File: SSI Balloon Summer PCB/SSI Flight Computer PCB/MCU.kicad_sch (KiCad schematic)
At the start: 27 parts, among them J5 Conn_01x05, J9 Camera, SW2 SW_SPST, SW3 SW_SPST, U7 STM32F411CEUx, Y1 ABM8W-12.0000MHZ-8-K1Z-T3

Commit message: Various rewiring: SWD, microSD, APRS JST
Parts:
- J5: value Conn_01x05 -> SWDIO
- SW1: renamed from SW2; value SW_SPST -> NRST
- SW2: renamed from SW3; value SW_SPST -> BOOT0
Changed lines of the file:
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@@
 			)
 		)
-		(property "Value" "Conn_01x05"
+		(property "Value" "SWDIO"
 			(at 292.1 210.82 0)
 			(show_name no)
@@
 		(dnp no)
 		(fields_autoplaced yes)
-		(property "Reference" "SW2"
+		(property "Reference" "SW1"
 			(at 349.25 218.4399 90)
 			(show_name no)
@@
 			)
 		)
-		(property "Value" "SW_SPST"
+		(property "Value" "NRST"
 			(at 349.25 220.9799 90)
 			(show_name no)
@@
 			(project "SSI Summer Balloons"
 				(path "/3c45a535-6e6b-4825-ad52-82c10cbe7866/b11ef58b-98ba-47ea-88cc-0eee30828228"
-					(reference "SW2")
+					(reference "SW1")
 					(unit 1)
 				)
@@
 		(dnp no)
 		(fields_autoplaced yes)
-		(property "Reference" "SW3"
+		(property "Reference" "SW2"
 			(at 379.73 209.5499 90)
 			(show_name no)
@@
 			)
 		)
-		(property "Value" "SW_SPST"
+		(property "Value" "BOOT0"
 			(at 379.73 212.0899 90)
 			(show_name no)
@@
 			(project "SSI Summer Balloons"
 				(path "/3c45a535-6e6b-4825-ad52-82c10cbe7866/b11ef58b-98ba-47ea-88cc-0eee30828228"
-					(reference "SW3")
+					(reference "SW2")
 					(unit 1)
 				)

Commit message: Cleaned APRS Filter up and adding Testing points
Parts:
- removed C48: 1nF, Capacitor_SMD:C_0603_1608Metric, symbol Device:C
- removed R31: 47k, Resistor_SMD:R_0603_1608Metric, symbol Device:R
- added TP10, TP5, TP6, TP9: TestPoint, TestPoint:TestPoint_Pad_1.5x1.5mm, symbol Connector:TestPoint
- C47: value 10nF -> 22nF
- R30: value 4.7k -> 1k
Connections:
- net APRS_AUDIO: now also C47.1, R30.2, TP6.1
- net GND: now also TP5.1
- net NRST: now also TP10.1
- net APRS_PWM: now reaches R30.1, U7.10 (PA0)
- net APRS_PWM: now also TP9.1
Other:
- moved on the sheet: C47, R30

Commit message: Finished test points
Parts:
- added TP14, TP15: TestPoint, TestPoint:TestPoint_Pad_1.5x1.5mm, symbol Connector:TestPoint
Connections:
- net APRS_PD: now also TP14.1
- net APRS_PTT: now also TP15.1
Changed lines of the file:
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@@
 	(wire
 		(pts
+			(xy 306.07 144.78) (xy 306.07 151.13)
+		)
+		(stroke
+			(width 0)
+			(type default)
+		)
+	)
+	(wire
+		(pts
 			(xy 334.01 34.29) (xy 340.36 34.29)
 		)
@@
 	(wire
 		(pts
+			(xy 289.56 144.78) (xy 289.56 151.13)
+		)
+		(stroke
+			(width 0)
+			(type default)
+		)
+	)
+	(wire
+		(pts
 			(xy 90.17 132.08) (xy 128.27 132.08)
 		)
@@
 		)
 	)
+	(label "APRS_PD"
+		(at 289.56 151.13 0)
+		(effects
+			(font
+				(size 1.27 1.27)
+			)
+			(justify left bottom)
+		)
+	)
 	(label "SCK"
 		(at 180.34 101.6 0)
@@
 		)
 	)
+	(label "APRS_PTT"
+		(at 306.07 151.13 0)
+		(effects
+			(font
+				(size 1.27 1.27)
+			)
+			(justify left bottom)
+		)
+	)
 	(hierarchical_label "MOSI"
 		(shape output)
@@
 	)
 	(symbol
+		(lib_id "Connector:TestPoint")
+		(at 289.56 144.78 0)
+		(unit 1)
+		(body_style 1)
+		(exclude_from_sim no)
+		(in_bom yes)
+		(on_board yes)
+		(in_pos_files yes)
+		(dnp no)
+		(fields_autoplaced yes)
+		(property "Reference" "TP14"
+			(at 292.1 140.2079 0)
+			(show_name no)
+			(do_not_autoplace no)
+			(effects
+				(font
+					(size 1.27 1.27)
+				)
+				(justify left)
+			)
+		)
+		(property "Value" "TestPoint"
+			(at 292.1 142.7479 0)
+			(show_name no)
+			(do_not_autoplace no)
+			(effects
+				(font
+					(size 1.27 1.27)
+				)
+				(justify left)
+			)
+		)
+		(property "Footprint" "TestPoint:TestPoint_Pad_1.5x1.5mm"
+			(at 294.64 144.78 0)
+			(hide yes)
+			(show_name no)
+			(do_not_autoplace no)
+			(effects
+				(font
+					(size 1.27 1.27)
+				)
+			)
+		)
+		(property "Datasheet" ""
+			(at 294.64 144.78 0)
+			(hide yes)
+			(show_name no)
+			(do_not_autoplace no)
+			(effects
+				(font
+					(size 1.27 1.27)
+				)
+			)
+		)
+		(property "Description" "test point"
+			(at 289.56 144.78 0)
+			(hide yes)
+			(show_name no)
+			(do_not_autoplace no)
+			(effects
+				(font
+					(size 1.27 1.27)
+				)
+			)
+		)
+		(property "PART_REV" ""
+			(at 289.56 144.78 0)
+			(hide yes)
+			(show_name no)
+			(do_not_autoplace no)
+			(effects
+				(font
+					(size 1.27 1.27)
+				)
+			)
+		)
+		(pin "1"
+		)
+		(instances
+			(project "SSI Summer Balloons"
+				(path "/3c45a535-6e6b-4825-ad52-82c10cbe7866/b11ef58b-98ba-47ea-88cc-0eee30828228"
+					(reference "TP14")
+					(unit 1)
+				)
+			)
+		)
+	)
+	(symbol
 		(lib_id "Device:C")
 		(at 191.77 68.58 0)
@@
 					(unit 1)
 				)
+			)
+		)
+	)
+	(symbol
+		(lib_id "Connector:TestPoint")
+		(at 306.07 144.78 0)
+		(unit 1)
+		(body_style 1)
+		(exclude_from_sim no)
+		(in_bom yes)
+		(on_board yes)
+		(in_pos_files yes)
+		(dnp no)
+		(fields_autoplaced yes)
+		(property "Reference" "TP15"
+			(at 308.61 140.2079 0)
+			(show_name no)
+			(do_not_autoplace no)
+			(effects
+				(font
+					(size 1.27 1.27)
+				)
+				(justify left)
+			)
+		)
+		(property "Value" "TestPoint"
+			(at 308.61 142.7479 0)
+			(show_name no)
+			(do_not_autoplace no)
+			(effects
+				(font
+					(size 1.27 1.27)
+				)
+				(justify left)
+			)
+		)
+		(property "Footprint" "TestPoint:TestPoint_Pad_1.5x1.5mm"
+			(at 311.15 144.78 0)
+			(hide yes)
+			(show_name no)
+			(do_not_autoplace no)
+			(effects
+				(font
+					(size 1.27 1.27)
+				)
+			)
+		)
+		(property "Datasheet" ""
+			(at 311.15 144.78 0)
+			(hide yes)
+			(show_name no)
+			(do_not_autoplace no)
+			(effects
+				(font
+					(size 1.27 1.27)
+				)
+			)
+		)
+		(property "Description" "test point"
+			(at 306.07 144.78 0)
+			(hide yes)
+			(show_name no)
+			(do_not_autoplace no)
+			(effects
+				(font
+					(size 1.27 1.27)
+				)
+			)
+		)
+		(property "PART_REV" ""
+			(at 306.07 144.78 0)
+			(hide yes)
+			(show_name no)
+			(do_not_autoplace no)
+			(effects
+				(font
+					(size 1.27 1.27)
+				)
+			)
+		)
+		(pin "1"
+		)
+		(instances
+			(project "SSI Summer Balloons"
+				(path "/3c45a535-6e6b-4825-ad52-82c10cbe7866/b11ef58b-98ba-47ea-88cc-0eee30828228"
+					(reference "TP15")
+					(unit 1)
+				)

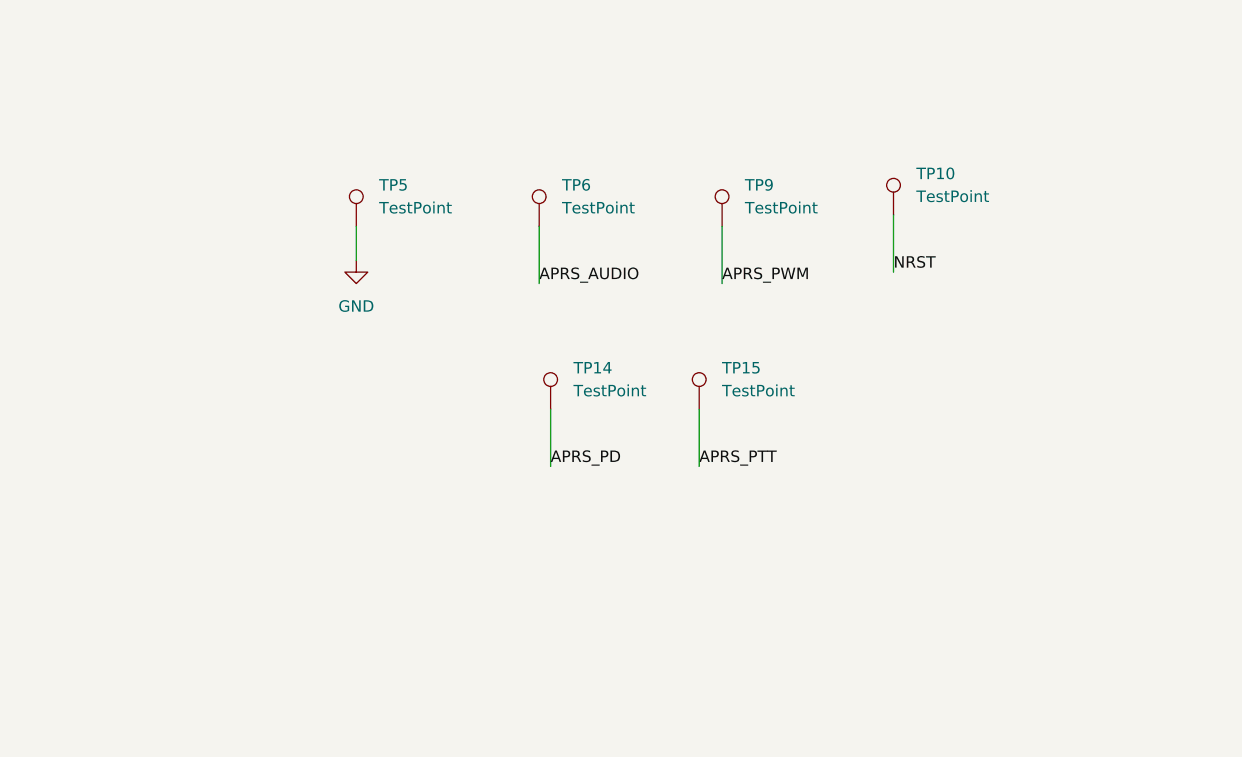
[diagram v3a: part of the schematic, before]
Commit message: Added Headers for testing, finalizing PCB
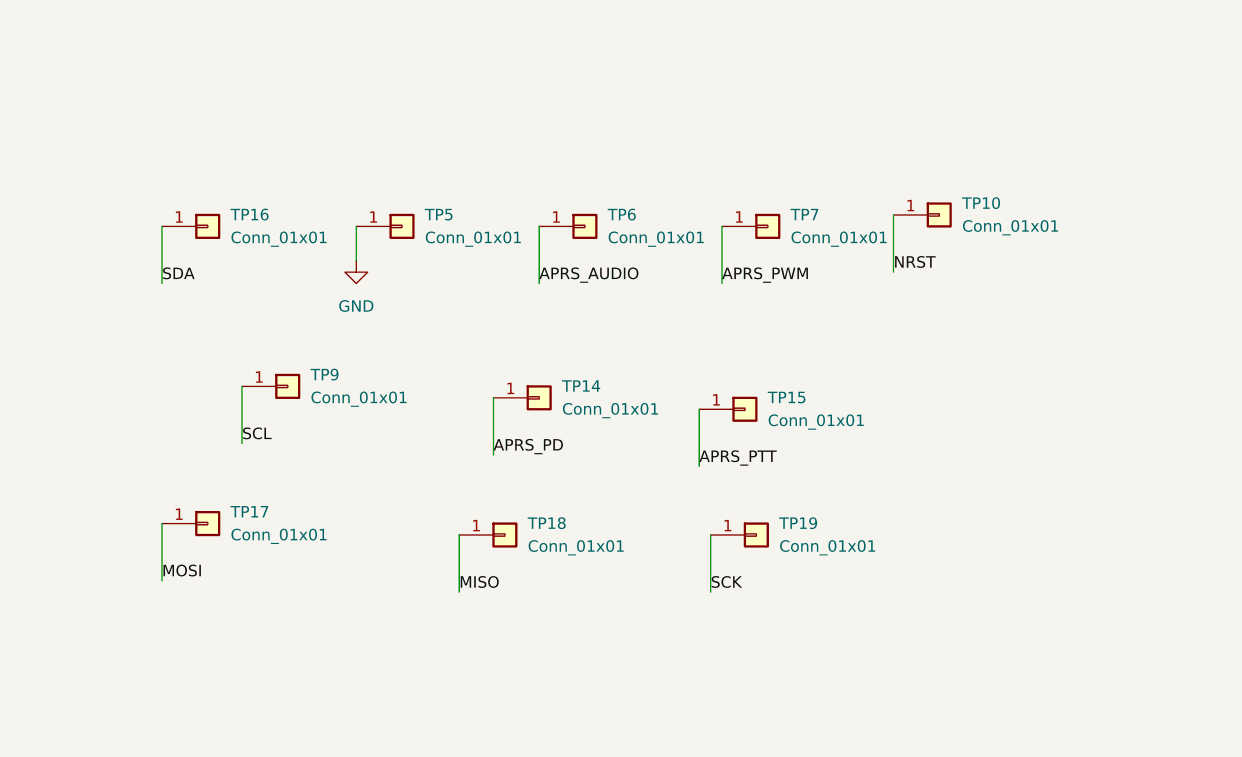
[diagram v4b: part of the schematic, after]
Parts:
- removed TP10, TP14, TP15, TP5, TP6, TP9: TestPoint, TestPoint:TestPoint_Pad_1.5x1.5mm, symbol Connector:TestPoint
- added TP10, TP14, TP15, TP16, TP17, TP18, TP19, TP5, TP6, TP7, TP9: Conn_01x01, Connector_PinHeader_2.54mm:PinHeader_1x01_P2.54mm_Vertical, symbol Connector_Generic:Conn_01x01
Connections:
- net APRS_AUDIO: now also TP6.1 (Pin_1)
- net APRS_PD: now also TP14.1 (Pin_1)
- net APRS_PTT: now also TP15.1 (Pin_1)
- net APRS_PWM: now also TP7.1 (Pin_1)
- net GND: now also TP5.1 (Pin_1)
- net MISO: now also TP18.1 (Pin_1)
- net MOSI: now also TP17.1 (Pin_1)
- net NRST: now also TP10.1 (Pin_1)
- net SCK: now also TP19.1 (Pin_1)
- net SCL: now also TP9.1 (Pin_1)
- net SDA: now also TP16.1 (Pin_1)

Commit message: More silkscreen organization, combined some pinheaders
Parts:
- removed TP16, TP17, TP18, TP19, TP9: Conn_01x01, Connector_PinHeader_2.54mm:PinHeader_1x01_P2.54mm_Vertical, symbol Connector_Generic:Conn_01x01
- added J11: SPI, Connector_PinHeader_2.54mm:PinHeader_1x03_P2.54mm_Vertical, symbol Connector_Generic:Conn_01x03
- added J4: I2C, Connector_PinHeader_2.54mm:PinHeader_1x02_P2.54mm_Vertical, symbol Connector_Generic:Conn_01x02
- J9: value Camera -> CAM_CONN
- TP10: value Conn_01x01 -> NRST
- TP14: value Conn_01x01 -> APRS_PD
- TP15: value Conn_01x01 -> APRS_PT
- TP5: value Conn_01x01 -> GND
- TP6: value Conn_01x01 -> APRS_AUDIO
- TP7: value Conn_01x01 -> APRS_PWM
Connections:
- net MISO: now also J11.2 (Pin_2)
- net MOSI: now also J11.3 (Pin_3)
- net SCK: now also J11.1 (Pin_1)
- net SCL: now also J4.1 (Pin_1)
- net SDA: now also J4.2 (Pin_2)

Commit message: finished finding all parts on JLCPCB - finalizing BOM then order
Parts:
- C24, C25, C26, C29, C49: LCSC (none) -> C519438
- C27, C28: LCSC (none) -> C76639
- C30: LCSC (none) -> C92806
- C31, C32: LCSC (none) -> C1685
- C33: value 0.1uF -> 100nF; LCSC (none) -> C519438
- C47: LCSC (none) -> C5128373
- J11: LCSC (none) -> C49257
- J4: LCSC (none) -> C168673
- J5: LCSC (none) -> C5156614
- J9: footprint Connector_PinHeader_2.54mm:PinHeader_1x08_P2.54mm_Vertical -> Connector_JST:JST_XH_B8B-XH-A_1x08_P2.50mm_Vertical; LCSC (none) -> C161875
- R13: value R_EXT -> 0; LCSC (none) -> C21189
- R14, R15, R27: LCSC (none) -> C25804
- R28, R29: LCSC (none) -> C23162
- R30: LCSC (none) -> C21190
- SW1, SW2: LCSC (none) -> C110293
- TP10, TP14, TP15, TP5, TP6, TP7: LCSC (none) -> C81276
- U7: LCSC (none) -> C190642
- Y1: LCSC (none) -> C1985370

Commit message: PCB finally done i think and ready to order
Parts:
- added D1: LED, LED_SMD:LED_0805_2012Metric, symbol Device:LED
- added R18: 330, Resistor_SMD:R_0603_1608Metric, symbol Device:R
- C24, C25, C26, C29, C33, C49: LCSC C519438 -> C14663
- C30: LCSC C92806 -> C29936
- R28, R29: LCSC C23162 -> C98195
- U7: LCSC C190642 -> C60420
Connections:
- net GND: now also D1.1 (K)
- net at U7.41 (PB5): now also R18.1
- new net: D1.2 (A), R18.2
- no-connect marks 10 -> 9

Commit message: Board done but we have a price crisis so might have to change things
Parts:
- added D3: LED, LED_SMD:LED_0805_2012Metric, symbol Device:LED
- added R32: 1k, Resistor_SMD:R_0603_1608Metric, symbol Device:R
- C47: LCSC C5128373 -> C49326627
- D1: LCSC C84256 -> C2297
- J11, J4, J5, TP10, TP14, TP15, TP5, TP6, TP7: now not fitted; now left out of the parts list
- R18: value 330 -> 150; LCSC C23138 -> C22808
- SW1, SW2: footprint Button_Switch_SMD:SW_Push_1P1T-MP_NO_Horizontal_Alps_SKRTLAE010 -> Button_Switch_SMD:SW_SPST_B3U-1000P; LCSC C110293 -> C720477
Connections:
- net +3V3: now also D3.2 (A)
- net GND: now also R32.1
- new net: D3.1 (K), R32.2
